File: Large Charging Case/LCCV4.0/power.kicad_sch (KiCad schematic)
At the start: 51 parts, among them J23 USB_C_Receptacle_USB2.0, J29 Conn_01x03, U16 ETA9882, U22 ME6215, U4 MT9700

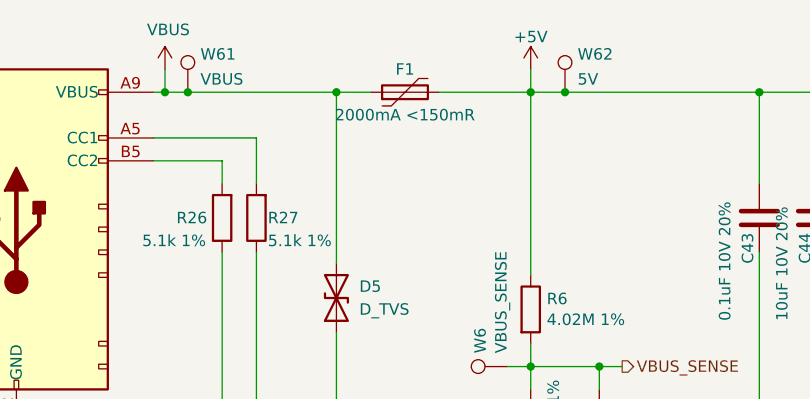
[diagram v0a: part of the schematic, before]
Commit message: Super6, LCCV4 updates and Kicad8
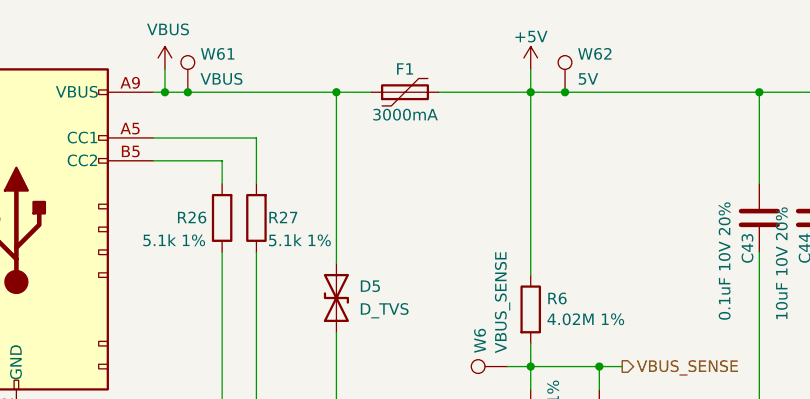
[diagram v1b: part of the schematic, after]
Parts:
- F1: value 2000mA <150mR -> 3000mA; LCSC Part Number (none) -> C22379947; Manufacturer Shenzhen JDT Fuse -> LUTE; Manufacturer Part Number ASMD1210-110-16V -> 1210L300/24WR
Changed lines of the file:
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@@
       (effects (font (size 1.27 1.27)))
     )
-    (property "Value" "2000mA <150mR" (at 68.58 38.1 90)
+    (property "Value" "3000mA" (at 68.58 38.1 90)
       (effects (font (size 1.27 1.27)))
     )
@@
       (effects (font (size 1.27 1.27)) hide)
     )
-    (property "Manufacturer" "Shenzhen JDT Fuse" (at 68.58 35.56 0)
+    (property "Manufacturer" "LUTE" (at 68.58 35.56 0)
       (effects (font (size 1.27 1.27)) hide)
     )
@@
       (effects (font (size 1.27 1.27)) hide)
     )
-    (property "LCSC Part Number" "" (at 68.58 35.56 0)
+    (property "LCSC Part Number" "C22379947" (at 68.58 35.56 0)
       (effects (font (size 1.27 1.27)) hide)
     )
-    (property "Manufacturer Part Number" "ASMD1210-110-16V" (at 68.58 35.56 0)
+    (property "Manufacturer Part Number" "1210L300/24WR" (at 68.58 35.56 0)
       (effects (font (size 1.27 1.27)) hide)
     )
